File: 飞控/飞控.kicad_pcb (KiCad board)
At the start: 4 copper layers, 52 x 25 mm, 71 parts, among them J2 Conn_01x06_Pin, J3 Conn_01x03, J4 M1_OUT, J5 M2_OUT, J6 M3_OUT, J7 M4_OUT, Q1 AO3400A, Q2 AO3400A, Q3 AO3400A, Q4 AO3400A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

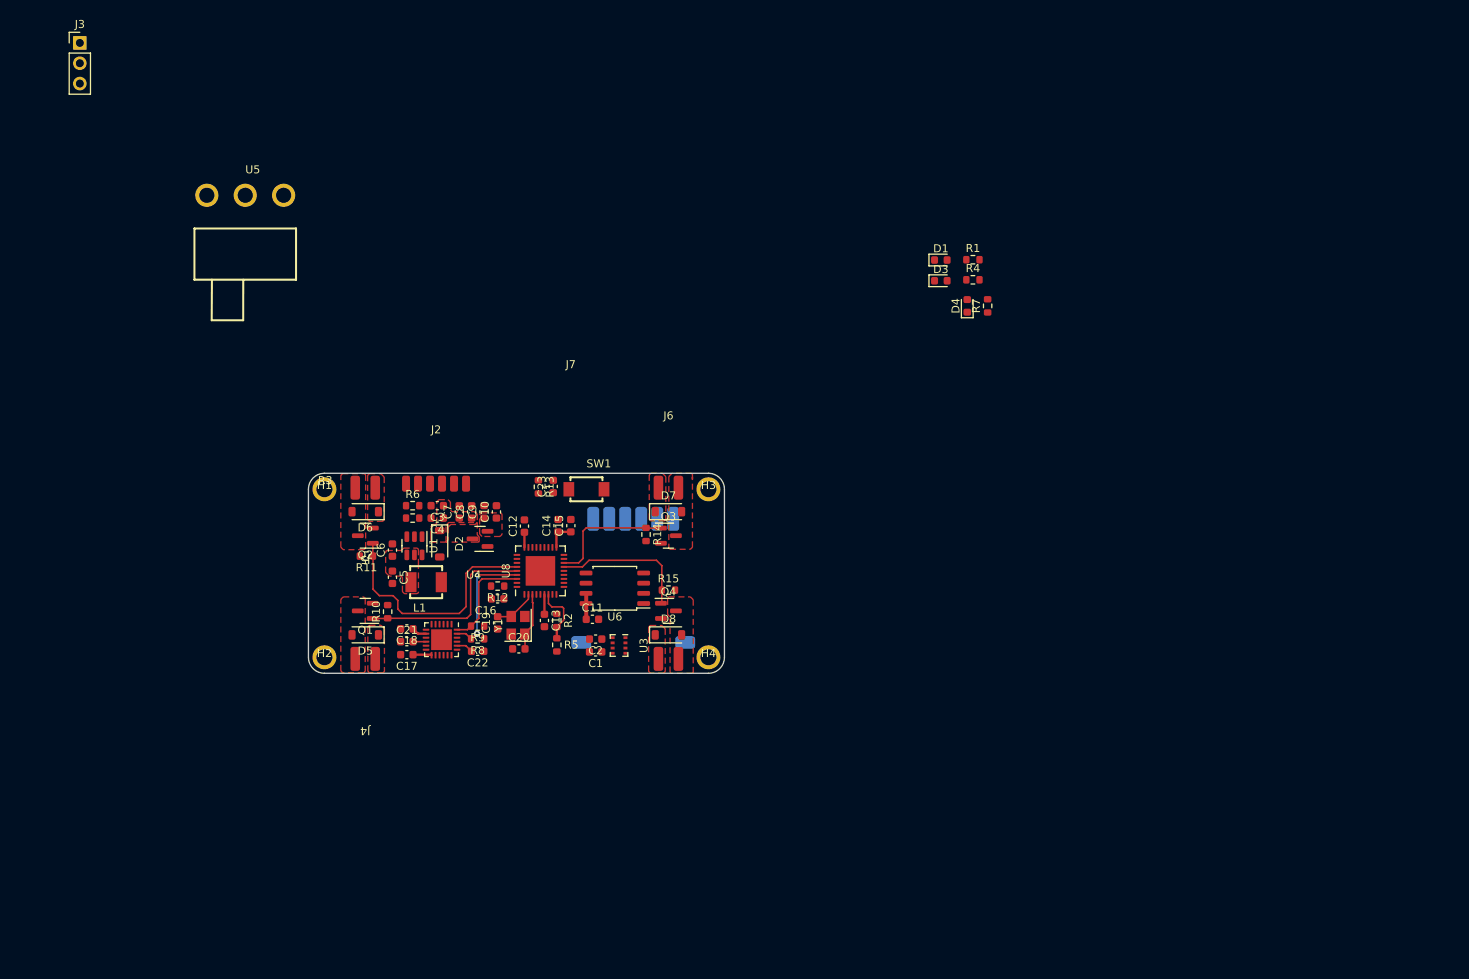
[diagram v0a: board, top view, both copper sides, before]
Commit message: 飞控pcb布局
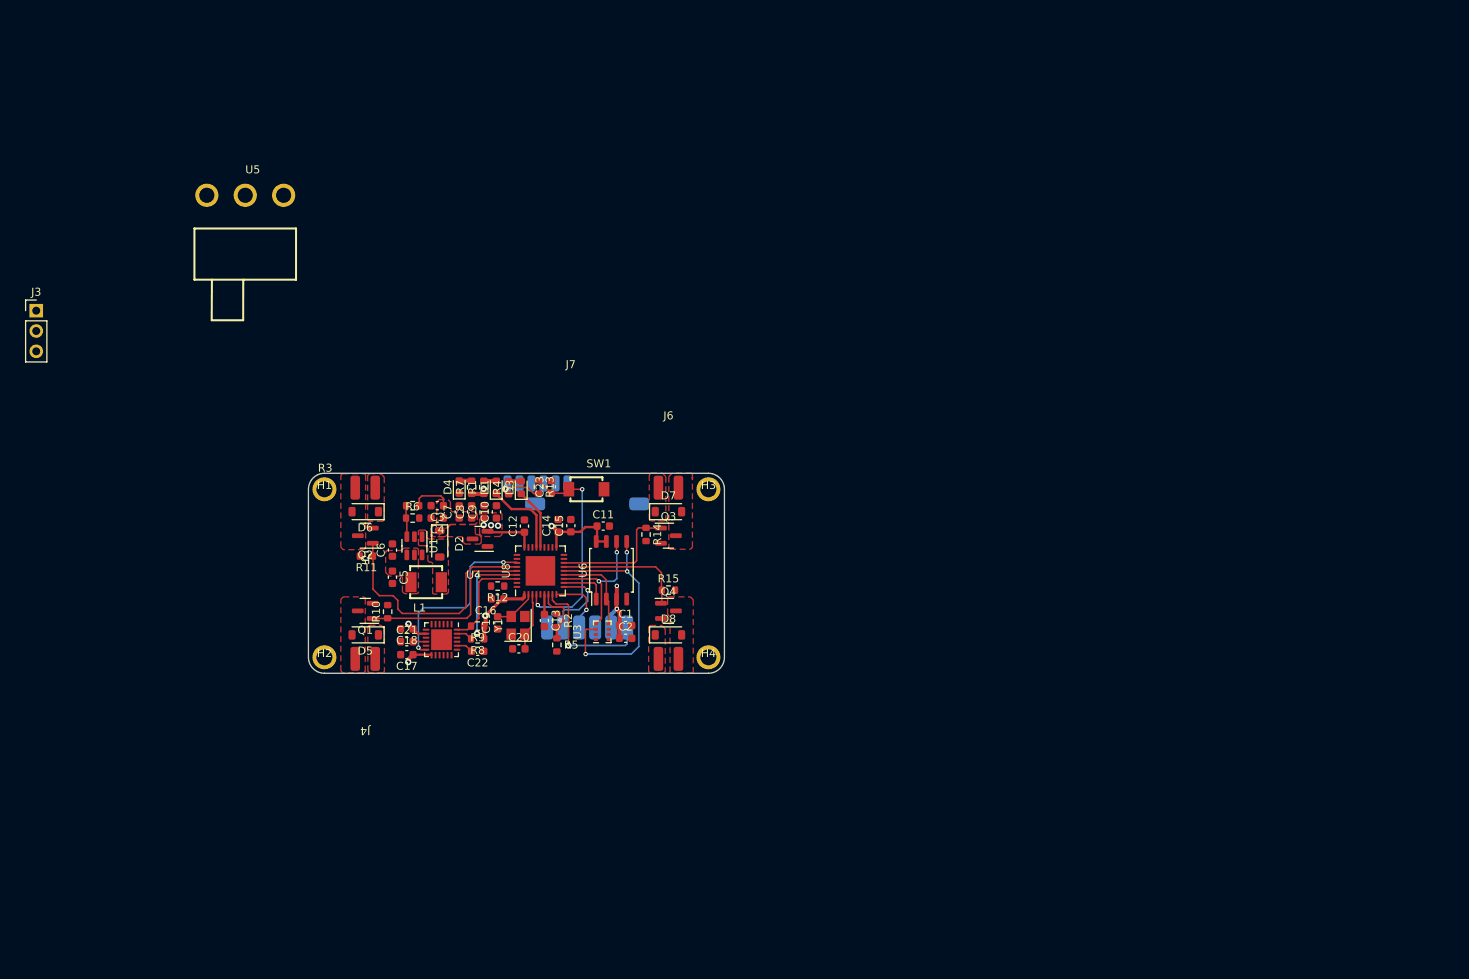
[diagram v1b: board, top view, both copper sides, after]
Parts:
- J2: moved to B.Cu
- moved R7 68.4 mm to (118.4, 99.8)
- moved R1 67.4 mm to (119.9, 99.8), turned to 90 degrees
- moved D4 67.4 mm to (116.8, 99.7)
- moved R4 63.6 mm to (123.0, 99.8), turned to 90 degrees
- moved D1 62.4 mm to (121.5, 99.8), turned to 90 degrees
- moved D3 58.5 mm to (124.6, 99.8), turned to 90 degrees
- moved J3 33.9 mm to (64.0, 77.7)
- moved J2 12.7 mm to (126.6, 99.3), turned to 180 degrees
- moved C11 11.7 mm to (134.8, 104.6)
- moved U2 8.26 mm to (132.8, 107.5), turned to 180 degrees
- moved C1 5.00 mm to (137.7, 117.0), turned to 0 degrees
- moved C2 3.75 mm to (137.7, 118.6), turned to 0 degrees
- moved U3 2.70 mm to (134.7, 117.8), turned to 90 degrees
- moved U6 2.29 mm to (135.9, 110.1), turned to 90 degrees
- moved R3 1.55 mm to (111.0, 102.0)
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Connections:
- net Net-(D2-A) renamed /SW
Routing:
- net +3.3V: track 15.5 -> 118.3 mm, vias 0 -> 11
- net /SPI_MOSI: track 0.00 -> 33.1 mm, vias 0 -> 3
- net /NRST: track 0.00 -> 27.4 mm, vias 0 -> 2
- net /6050_INT: track 0.00 -> 23.0 mm, vias 0 -> 2
- net /UART_RST: track 0.00 -> 17.5 mm, vias 0 -> 1
- net /SPI_SCK: track 0.00 -> 17.3 mm, vias 0 -> 2
- net /SPI_MISO: track 0.00 -> 11.2 mm
- net /U2_RX: track 0.00 -> 10.3 mm, vias 0 -> 1
- net /LED1: track 0.00 -> 10.2 mm
- net /U2_TX: track 0.00 -> 7.98 mm, vias 0 -> 1
- net /LED2: track 0.00 -> 7.69 mm
- net /SPI_CS: track 0.00 -> 5.91 mm
- net +5V: track 0.00 -> 5.09 mm
- net /FB: track 0.00 -> 3.92 mm
- net Net-(D3-A): track 0.00 -> 1.58 mm
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- added copper zone on F.Cu, net /SW

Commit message: 飞控修改
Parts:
- removed SW1: RST, Button_Switch_SMD:SW-SMD_L4.0-W2.9-LS4.8-1
- removed U5: SS12D06弯针, Button_Switch_THT:SW-TH_3P-SS12D06-1
- added CN1: ZH1.5-2P-WT, my_conn:CONN-SMD_ZH1.5-2P-WT, F.Cu at (145.8, 105.8)
- added J1: Conn_01x01_Pin, TestPoint:TestPoint_Pad_D1.0mm, F.Cu at (106.3, 92.9)
- added J10: Conn_01x01_Pin, TestPoint:TestPoint_Pad_D1.0mm, F.Cu at (112.4, 96.0)
- added J11: Conn_01x01_Pin, Connector_Wire:SolderWirePad_1x01_SMD_1x2mm, F.Cu at (102.7, 121.7)
- added J12: Conn_01x01_Pin, Connector_Wire:SolderWirePad_1x01_SMD_1x2mm, F.Cu at (125.0, 140.2)
- added J13: Conn_01x01_Pin, Connector_Wire:SolderWirePad_1x01_SMD_1x2mm, F.Cu at (127.4, 140.2)
- added J14: Conn_01x01_Pin, Connector_Wire:SolderWirePad_1x01_SMD_1x2mm, F.Cu at (129.7, 140.2)
- added J8: Conn_01x01_Pin, TestPoint:TestPoint_Pad_D1.0mm, F.Cu at (109.4, 96.0)
- added J9: Conn_01x01_Pin, TestPoint:TestPoint_Pad_D1.0mm, F.Cu at (112.4, 92.9)
- added SW2: MST22D18G2_125, my_switch:SW-SMD_MST22D18G2, F.Cu at (137.4, 109.6)
- added U9: ZX-ZH1.5-3PWT, my_conn:CONN-SMD_3P-P1.50_ZX-ZH1.5-3PWT, F.Cu at (146.1, 114.4)
- J2: value Conn_01x06_Pin -> Conn_01x01_Pin; footprint Connector_Wire:WirePad_1x06_1.5mm -> TestPoint:TestPoint_Pad_D1.0mm; moved to F.Cu
- J3: value Conn_01x03 -> Conn_01x01_Pin; footprint Connector_PinHeader_2.54mm:PinHeader_1x03_P2.54mm_Vertical -> TestPoint:TestPoint_Pad_D1.0mm
- J4: value M1_OUT -> Conn_01x01_Pin; footprint Connector_Wire:WIrePad_1x02_2mm -> Connector_Wire:SolderWirePad_1x01_SMD_1x2mm
- J5: value M2_OUT -> Conn_01x01_Pin; footprint Connector_Wire:WIrePad_1x02_2mm -> Connector_Wire:SolderWirePad_1x01_SMD_1x2mm
- J6: value M3_OUT -> Conn_01x01_Pin; footprint Connector_Wire:WIrePad_1x02_2mm -> Connector_Wire:SolderWirePad_1x01_SMD_1x2mm
- J7: value M4_OUT -> Conn_01x01_Pin; footprint Connector_Wire:WIrePad_1x02_2mm -> Connector_Wire:SolderWirePad_1x01_SMD_1x2mm
- L1: footprint Inductor_SMD:IND-SMD_L4.0-W4.0_0.47UH04209.5A -> Inductor_SMD:IND-SMD_L4.9-W4.4_MAPM0420F
- U2: footprint RF_Module:2.4G-UART -> my_module:2.4G-UART
- U6: moved to B.Cu
- moved C7 123.7 mm to (238.6, 124.6), turned to -90 degrees
- moved C8 120.6 mm to (237.0, 124.6), turned to -90 degrees
- moved U4 104.0 mm to (219.0, 136.1), turned to 0 degrees
- moved C9 92.5 mm to (210.5, 121.7), turned to 0 degrees
- moved C10 91.6 mm to (210.5, 124.2), turned to 0 degrees
- moved R3 88.2 mm to (192.1, 136.8), turned to 90 degrees
- moved C3 86.9 mm to (192.1, 140.4), turned to 90 degrees
- moved R6 86.0 mm to (190.4, 136.8), turned to -90 degrees
- moved C4 84.7 mm to (190.4, 140.4), turned to 90 degrees
- moved C6 82.6 mm to (186.8, 133.9), turned to 0 degrees
- moved U1 81.2 mm to (186.8, 137.1), turned to 180 degrees
- moved D2 80.2 mm to (187.1, 140.8), turned to 180 degrees
- moved C5 78.5 mm to (183.6, 133.9), turned to 180 degrees
- moved C1 76.7 mm to (62.7, 100.7)
- moved C2 76.5 mm to (62.7, 103.2)
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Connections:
- J2 pad 1: +3.3V -> /SWCLK
- J3 pad 1: +5V -> /SWDIO
- J7 pad 1: +BATT -> /M4
- U8 pad 33: /6050_SCL -> /6050_SDA
- U8 pad 34: /6050_SDA -> /6050_SCL
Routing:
- net +3.3V: track 118.3 -> 0.00 mm, vias 11 -> 0
- net /SPI_MOSI: track 33.1 -> 0.00 mm, vias 3 -> 0
- net /PWM1: track 30.5 -> 0.00 mm
- net /NRST: track 27.4 -> 0.00 mm, vias 2 -> 0
- net /PWM2: track 23.4 -> 0.00 mm
- net /6050_INT: track 23.0 -> 0.00 mm, vias 2 -> 0
- net /UART_RST: track 17.5 -> 0.00 mm, vias 1 -> 0
- net /SPI_SCK: track 17.3 -> 0.00 mm, vias 2 -> 0
- net /PWM4: track 16.4 -> 0.00 mm
- net /PWM3: track 16.2 -> 0.00 mm
- net /SPI_MISO: track 11.2 -> 0.00 mm
- net /U2_RX: track 10.3 -> 0.00 mm, vias 1 -> 0
- net /LED1: track 10.2 -> 0.00 mm
- net /U2_TX: track 7.98 -> 0.00 mm, vias 1 -> 0
- net /LED2: track 7.69 -> 0.00 mm
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- removed copper zone on F.Cu, net +3.3V
- removed copper zone on F.Cu, net +5V
- removed copper zone on F.Cu, net +BATT
- removed copper zone on F.Cu, net /M1
- removed copper zone on F.Cu, net /M2
- removed copper zone on F.Cu, net /M3
- removed copper zone on F.Cu, net /M4
- removed copper zone on F.Cu, net /SW
